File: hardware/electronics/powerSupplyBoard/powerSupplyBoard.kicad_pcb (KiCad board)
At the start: 4 copper layers, 100 x 50 mm, 119 parts, among them J1 USB_C_Receptacle_USB2.0, J10 1729018, J11 PREC002SAAN-RC, J3 615004143821, J4 PRPC009SBAN-M71RC, J5 Barrel_Jack_Switch, J6 S2B-PH-SM4-TB, J7 PREC002SAAN-RC, J8 PREC003SAAN-RC, J9 S3B-XH-SM4-TB, Q1 BUK961R6, Q2 CSD18532Q5B, Q3 CSD18532Q5B, Q4 BSS84, Q5 2N7002, Q6 2N7002, SW1 PTS647, SW2 SS-12D07, U1 STM32L052K6, U2 AP2112K-3.3, U3 SN65HVD230QDR, U4 BQ25798, U5 BQ76905, U6 BQ34Z100-R2, Y1 ECS-327ATQMV

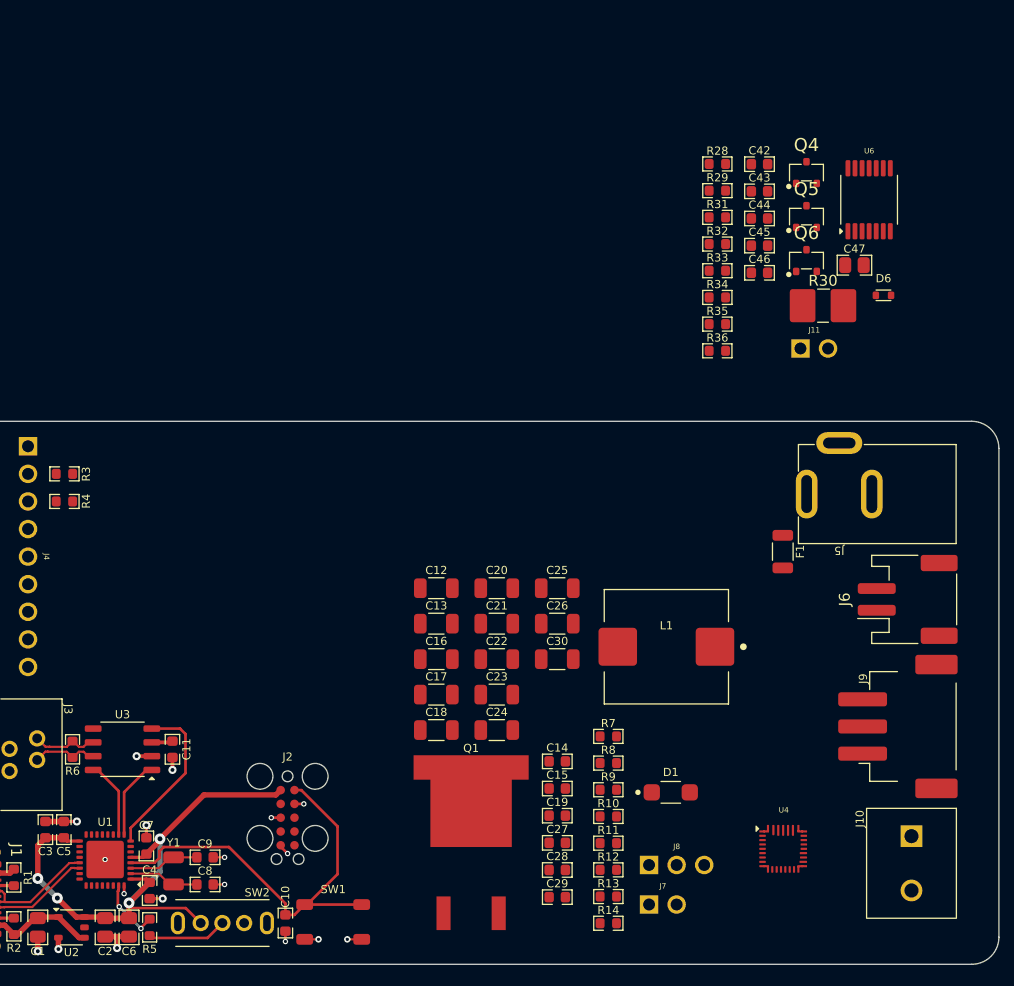
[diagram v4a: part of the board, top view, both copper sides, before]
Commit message: updated sch merger
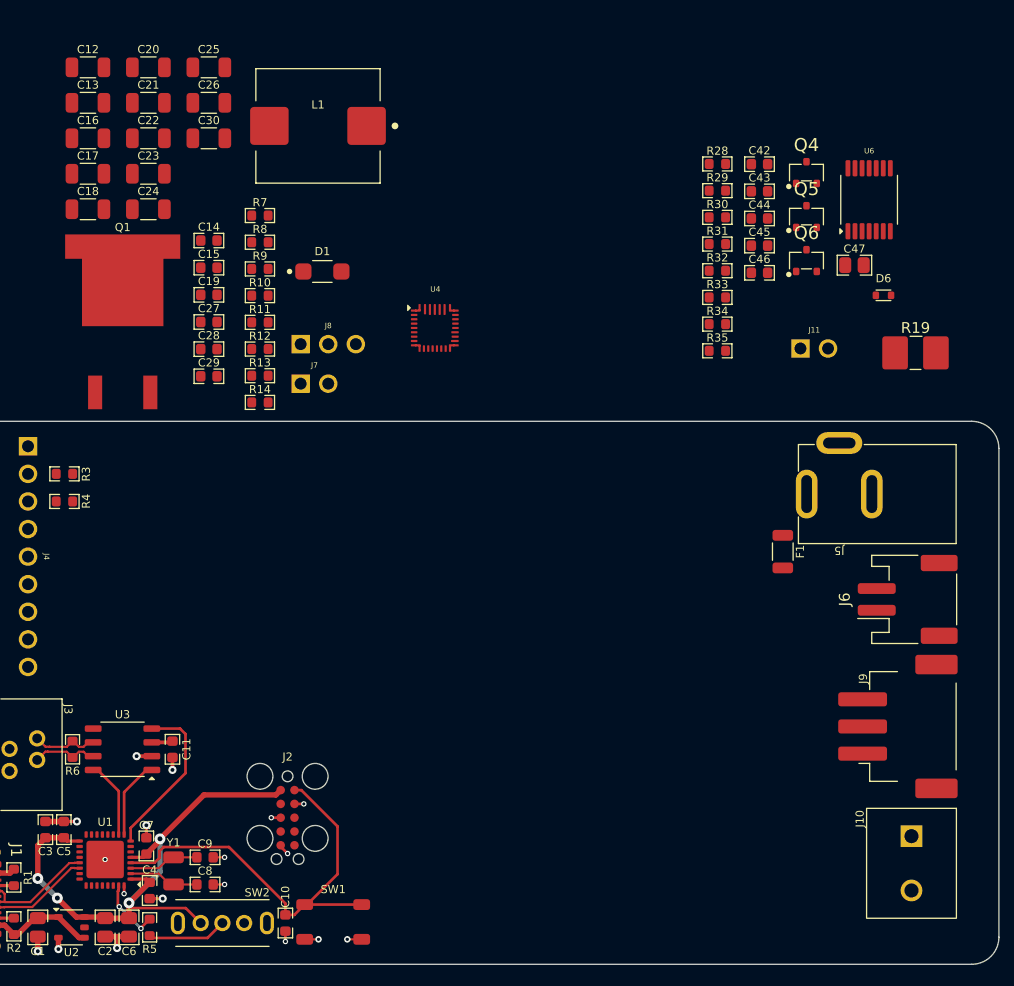
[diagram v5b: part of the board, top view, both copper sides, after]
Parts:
- removed the R30 at (168.8, 39.4)
- added R19: 30mR, DS-Resistors-SMD:WSLHP2010, F.Cu at (177.3, 43.7)
- moved C16 57.7 mm to (101.1, 23.9)
- moved C22 57.7 mm to (106.7, 23.9)
- moved C30 57.7 mm to (112.2, 23.9)
- moved J7 57.7 mm to (122.0, 46.5)
- moved Q1 57.7 mm to (104.3, 40.9)
- moved C13 57.7 mm to (101.1, 20.7)
- moved C14 57.7 mm to (112.3, 33.4)
- moved C15 57.7 mm to (112.3, 35.9)
- moved C18 57.7 mm to (101.1, 30.5)
- moved C19 57.7 mm to (112.3, 38.4)
- moved C21 57.7 mm to (106.7, 20.7)
- moved C24 57.7 mm to (106.7, 30.5)
- moved C26 57.7 mm to (112.2, 20.7)
- moved C27 57.7 mm to (112.3, 40.9)
- moved C28 57.7 mm to (112.3, 43.4)
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- renumbered R31 to R30, R32 to R31, R33 to R32, R34 to R33, R35 to R34, R36 to R35
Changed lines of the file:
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@@
 	(footprint "DS-Capacitors-SMD:MLCC1206"
 		(layer "F.Cu")
-		(at 133.198 75.166)
+		(at 101.118 27.206)
 		(descr "Capacitor, Chip; 3.20 mm L X 1.60 mm W X 0.88 mm H body")
 		(tags "1206; 3216")
@@
 	(footprint "DS-Capacitors-SMD:MLCC1206"
 		(layer "F.Cu")
-		(at 133.198 71.9)
+		(at 101.118 23.94)
 		(descr "Capacitor, Chip; 3.20 mm L X 1.60 mm W X 0.88 mm H body")
 		(tags "1206; 3216")
@@
 	(footprint "DS-Capacitors-SMD:MLCC0603"
 		(layer "F.Cu")
-		(at 144.335 88.815)
+		(at 112.255 40.855)
 		(descr "Capacitor, Chip; 1.60 mm L X 0.80 mm W X 0.88 mm H body")
 		(tags "0603; 1608")
@@
 	(footprint "DS-LED-SMD:LTST-1206"
 		(layer "F.Cu")
-		(at 154.785 84.165)
+		(at 122.705 36.205)
 		(descr "LED, Chip; 3.50 mm L X 2.20 mm W X 1.95 mm H body")
 		(property "Reference" "D1"
@@
 	(footprint "DS-Resistors-SMD:CRCW0603"
 		(layer "F.Cu")
-		(at 149.035 83.93)
+		(at 116.955 35.97)
 		(descr "Resistor, Chip; 1.60 mm L X 0.80 mm W X 0.55 mm H body")
 		(tags "0603; 1608")
@@
 	(footprint "DS-Resistors-SMD:CRCW0603"
 		(layer "F.Cu")
-		(at 149.035 86.388)
+		(at 116.955 38.428)
 		(descr "Resistor, Chip; 1.60 mm L X 0.80 mm W X 0.55 mm H body")
 		(tags "0603; 1608")
@@
 	(footprint "DS-Capacitors-SMD:MLCC1206"
 		(layer "F.Cu")
-		(at 138.764 75.166)
+		(at 106.684 27.206)
 		(descr "Capacitor, Chip; 3.20 mm L X 1.60 mm W X 0.88 mm H body")
 		(tags "1206; 3216")
@@
 	(footprint "DS-Resistors-SMD:WSLHP2010"
 		(layer "F.Cu")
-		(at 168.804 39.353)
+		(at 177.32 43.7)
 		(descr "Resistor, Chip; 5.08 mm L X 2.54 mm W X 0.889 mm H body")
-		(property "Reference" "R30"
+		(property "Reference" "R19"
 			(at 0 -2.3 0)
 			(layer "F.SilkS")
@@
 			)
 		)
-		(property "Value" "10mR"
+		(property "Value" "30mR"
 			(at 0 0 0)
 			(layer "User.1")
@@
 			)
 		)
-		(property "Description" "RES 0.01 OHM 1% 1W 2010"
+		(property "Description" "RES 0.03 OHM 1% 1W 2010"
 			(at 0 0 0)
 			(layer "F.Fab")
@@
 			)
 		)
-		(property "MPN" "WSL2010R0100FEA18"
+		(property "MPN" "WSL2010R0300FEA18"
 			(at 0 0 0)
 			(unlocked yes)
@@
 			)
 		)
-		(property "DKPN" "WSLF-.01CT-ND"
+		(property "DKPN" "WSLF-.03CT-ND"
 			(at 0 0 0)
 			(unlocked yes)
@@
 			)
 		)
-		(sheetname "Fuel Gauge")
-		(sheetfile "fuel_gauge.kicad_sch")
+		(sheetname "Battery Monitor")
+		(sheetfile "battery_monitor.kicad_sch")
 		(attr smd)
 		(fp_line
@@
 			(layers "F.Cu" "F.Paste" "F.Mask")
 			(roundrect_rratio 0.1059322034)
-			(net 23 "SENSE-")
+			(net 100 "SENSE+")
 			(pintype "passive")
 		)
@@
 			(layers "F.Cu" "F.Paste" "F.Mask")
 			(roundrect_rratio 0.1059322034)
-			(net 100 "SENSE+")
+			(net 23 "SENSE-")
 			(pintype "passive")
 		)
@@
 	(footprint "DS-Resistors-SMD:CRCW0603"
 		(layer "F.Cu")
-		(at 149.035 91.304)
+		(at 116.955 43.344)
 		(descr "Resistor, Chip; 1.60 mm L X 0.80 mm W X 0.55 mm H body")
 		(tags "0603; 1608")
@@
 		(descr "Resistor, Chip; 1.60 mm L X 0.80 mm W X 0.55 mm H body")
 		(tags "0603; 1608")
-		(property "Reference" "R36"
+		(property "Reference" "R35"
 			(at 0 -1.2 0)
 			(layer "F.SilkS")
@@
 	(footprint "DS-Capacitors-SMD:MLCC0603"
 		(layer "F.Cu")
-		(at 144.335 81.315)
+		(at 112.255 33.355)
 		(descr "Capacitor, Chip; 1.60 mm L X 0.80 mm W X 0.88 mm H body")
 		(tags "0603; 1608")
@@
 	(footprint "DS-Resistors-SMD:CRCW0603"
 		(layer "F.Cu")
-		(at 149.035 88.846)
+		(at 116.955 40.886)
 		(descr "Resistor, Chip; 1.60 mm L X 0.80 mm W X 0.55 mm H body")
 		(tags "0603; 1608")
@@
 	(footprint "DS-PMIC-SMD:RQM0029A"
 		(layer "F.Cu")
-		(at 165.135 89.365)
+		(at 133.055 41.405)
 		(property "Reference" "U4"
 			(at 0.05 -3.57 0)
@@
 	(footprint "DS-Capacitors-SMD:MLCC1206"
 		(layer "F.Cu")
-		(at 133.198 68.634)
+		(at 101.118 20.674)
 		(descr "Capacitor, Chip; 3.20 mm L X 1.60 mm W X 0.88 mm H body")
 		(tags "1206; 3216")
@@
 		(descr "Resistor, Chip; 1.60 mm L X 0.80 mm W X 0.55 mm H body")
 		(tags "0603; 1608")
-		(property "Reference" "R35"
+		(property "Reference" "R34"
 			(at 0 -1.2 0)
 			(layer "F.SilkS")
@@
 		(descr "Resistor, Chip; 1.60 mm L X 0.80 mm W X 0.55 mm H body")
 		(tags "0603; 1608")
-		(property "Reference" "R32"
+		(property "Reference" "R31"
 			(at 0 -1.2 0)
 			(layer "F.SilkS")
@@
 	(footprint "DS-Package-SO:SOT404"
 		(layer "F.Cu")
-		(at 136.4 88.9)
+		(at 104.32 40.94)
 		(property "Reference" "Q1"
 			(at 0 -8.8 0)
@@
 	(footprint "DS-Resistors-SMD:CRCW0603"
 		(layer "F.Cu")
-		(at 149.035 79.014)
+		(at 116.955 31.054)
 		(descr "Resistor, Chip; 1.60 mm L X 0.80 mm W X 0.55 mm H body")
 		(tags "0603; 1608")
@@
 	(footprint "DS-Capacitors-SMD:MLCC1206"
 		(layer "F.Cu")
-		(at 133.198 78.432)
+		(at 101.118 30.472)
 		(descr "Capacitor, Chip; 3.20 mm L X 1.60 mm W X 0.88 mm H body")
 		(tags "1206; 3216")
@@
 	(footprint "DS-Capacitors-SMD:MLCC1206"
 		(layer "F.Cu")
-		(at 133.198 65.368)
+		(at 101.118 17.408)
 		(descr "Capacitor, Chip; 3.20 mm L X 1.60 mm W X 0.88 mm H body")
 		(tags "1206; 3216")
@@
 	(footprint "DS-Capacitors-SMD:MLCC1206"
 		(layer "F.Cu")
-		(at 144.33 71.9)
+		(at 112.25 23.94)
 		(descr "Capacitor, Chip; 3.20 mm L X 1.60 mm W X 0.88 mm H body")
 		(tags "1206; 3216")
@@
 	(footprint "DS-Capacitors-SMD:MLCC1206"
 		(layer "F.Cu")
-		(at 138.764 65.368)
+		(at 106.684 17.408)
 		(descr "Capacitor, Chip; 3.20 mm L X 1.60 mm W X 0.88 mm H body")
 		(tags "1206; 3216")
@@
 	(footprint "DS-Capacitors-SMD:MLCC1206"
 		(layer "F.Cu")
-		(at 138.764 68.634)
+		(at 106.684 20.674)
 		(descr "Capacitor, Chip; 3.20 mm L X 1.60 mm W X 0.88 mm H body")
 		(tags "1206; 3216")
@@
 	(footprint "DS-Capacitors-SMD:MLCC0603"
 		(layer "F.Cu")
-		(at 144.335 86.315)
+		(at 112.255 38.355)
 		(descr "Capacitor, Chip; 1.60 mm L X 0.80 mm W X 0.88 mm H body")
 		(tags "0603; 1608")
@@
 		(descr "Resistor, Chip; 1.60 mm L X 0.80 mm W X 0.55 mm H body")
 		(tags "0603; 1608")
-		(property "Reference" "R34"
+		(property "Reference" "R33"
 			(at 0 -1.2 0)
 			(layer "F.SilkS")
@@
 	(footprint "DS-Capacitors-SMD:MLCC0603"
 		(layer "F.Cu")
-		(at 144.335 93.815)
+		(at 112.255 45.855)
 		(descr "Capacitor, Chip; 1.60 mm L X 0.80 mm W X 0.88 mm H body")
 		(tags "0603; 1608")
@@
 	(footprint "DS-Capacitors-SMD:MLCC1206"
 		(layer "F.Cu")
-		(at 138.764 71.9)
+		(at 106.684 23.94)
 		(descr "Capacitor, Chip; 3.20 mm L X 1.60 mm W X 0.88 mm H body")
 		(tags "1206; 3216")
@@
 	(footprint "DS-Capacitors-SMD:MLCC1206"
 		(layer "F.Cu")
-		(at 138.764 78.432)
+		(at 106.684 30.472)
 		(descr "Capacitor, Chip; 3.20 mm L X 1.60 mm W X 0.88 mm H body")
 		(tags "1206; 3216")
@@
 	(footprint "DS-Resistors-SMD:CRCW0603"
 		(layer "F.Cu")
-		(at 149.035 81.472)
+		(at 116.955 33.512)
 		(descr "Resistor, Chip; 1.60 mm L X 0.80 mm W X 0.55 mm H body")
 		(tags "0603; 1608")
@@
 	(footprint "DS-Rectangular-Connectors:conn_01x03_254"
 		(layer "F.Cu")
-		(at 155.325 90.855)
+		(at 123.245 42.895)
 		(property "Reference" "J8"
 			(at 0 -1.7 0)
@@
 	(footprint "DS-Capacitors-SMD:MLCC1206"
 		(layer "F.Cu")
-		(at 144.33 68.634)
+		(at 112.25 20.674)
 		(descr "Capacitor, Chip; 3.20 mm L X 1.60 mm W X 0.88 mm H body")
 		(tags "1206; 3216")
@@
 	(footprint "DS-Resistors-SMD:CRCW0603"
 		(layer "F.Cu")
-		(at 149.035 93.762)
+		(at 116.955 45.802)
 		(descr "Resistor, Chip; 1.60 mm L X 0.80 mm W X 0.55 mm H body")
 		(tags "0603; 1608")
@@
 	(footprint "DS-Capacitors-SMD:MLCC0603"
 		(layer "F.Cu")
-		(at 144.335 91.315)
+		(at 112.255 43.355)
 		(descr "Capacitor, Chip; 1.60 mm L X 0.80 mm W X 0.88 mm H body")
 		(tags "0603; 1608")
@@
 	(footprint "DS-Rectangular-Connectors:conn_01x02_254"
 		(layer "F.Cu")
-		(at 154.055 94.495)
+		(at 121.975 46.535)
 		(property "Reference" "J7"
 			(at 0 -1.7 0)
@@
 	(footprint "DS-Capacitors-SMD:MLCC0603"
 		(layer "F.Cu")
-		(at 144.335 83.815)
+		(at 112.255 35.855)
 		(descr "Capacitor, Chip; 1.60 mm L X 0.80 mm W X 0.88 mm H body")
 		(tags "0603; 1608")
@@
 	(footprint "DS-Resistors-SMD:CRCW0603"
 		(layer "F.Cu")
-		(at 149.035 96.22)
+		(at 116.955 48.26)
 		(descr "Resistor, Chip; 1.60 mm L X 0.80 mm W X 0.55 mm H body")
 		(tags "0603; 1608")
@@
 	(footprint "DS-Capacitors-SMD:MLCC1206"
 		(layer "F.Cu")
-		(at 144.33 65.368)
+		(at 112.25 17.408)
 		(descr "Capacitor, Chip; 3.20 mm L X 1.60 mm W X 0.88 mm H body")
 		(tags "1206; 3216")
@@
 	(footprint "DS-Inductors-SMD:HCM1A1105V2"
 		(layer "F.Cu")
-		(at 154.38 70.76)
+		(at 122.3 22.8)
 		(descr "Inductor, Chip; 2.50 mm L X 2.00 mm W X 1.20 mm H body")
 		(property "Reference" "L1"
@@
 		(descr "Resistor, Chip; 1.60 mm L X 0.80 mm W X 0.55 mm H body")
 		(tags "0603; 1608")
-		(property "Reference" "R33"
+		(property "Reference" "R32"
 			(at 0 -1.2 0)
 			(layer "F.SilkS")
@@
 		(descr "Resistor, Chip; 1.60 mm L X 0.80 mm W X 0.55 mm H body")
 		(tags "0603; 1608")
-		(property "Reference" "R31"
+		(property "Reference" "R30"
 			(at 0 -1.2 0)
 			(layer "F.SilkS")

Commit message: fixed GPIO header power net
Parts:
- R32: value 165K -> 14K
- R33: value 133K -> 100K
- R34: value 16K5 -> 14K
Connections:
- J4 pad 1: /VUSB -> +3V3
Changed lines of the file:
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@@
 			(layers "*.Cu" "*.Mask")
 			(remove_unused_layers no)
-			(net 88 "/VUSB")
+			(net 3 "+3V3")
 			(pintype "passive")
 		)
@@
 			)
 		)
-		(property "Value" "16K5"
+		(property "Value" "14K"
 			(at 0 0 0)
 			(layer "User.1")
@@
 			)
 		)
-		(property "Description" "RES 16.5K OHM 0.1% 0.21W 0603"
+		(property "Description" "RES 14K OHM 0.1% 0.21W 0603"
 			(at 0 0 0)
 			(layer "F.Fab")
@@
 			)
 		)
-		(property "MPN" "TNPW060316K5BEEA"
+		(property "MPN" "TNPW060314K0BEEA"
 			(at 0 0 0)
 			(unlocked yes)
@@
 			)
 		)
-		(property "DKPN" "541-3172-1-ND"
+		(property "DKPN" "TNP14.0KAACT-ND"
 			(at 0 0 0)
 			(unlocked yes)
@@
 			)
 		)
-		(property "Value" "133K"
+		(property "Value" "100K"
 			(at 0 0 0)
 			(layer "User.1")
@@
 			)
 		)
-		(property "Description" "RES 133K OHM 0.1% 0.21W 0603"
+		(property "Description" "RES 100K OHM 0.1% 0.21W 0603"
 			(at 0 0 0)
 			(layer "F.Fab")
@@
 			)
 		)
-		(property "MPN" "TNPW0603133KBEEA"
+		(property "MPN" "TNPW0603100KBEEA"
 			(at 0 0 0)
 			(unlocked yes)
@@
 			)
 		)
-		(property "DKPN" "541-TNPW0603133KBEEACT-ND"
+		(property "DKPN" "TNP100KAACT-ND"
 			(at 0 0 0)
 			(unlocked yes)
@@
 			)
 		)
-		(property "Datasheet" "datasheets/Texas-Instruments-BQ34Z100-R2"
+		(property "Datasheet" "datasheets/Texas-Instruments-BQ34Z100-R2.pdf"
 			(at 0 0 0)
 			(layer "F.Fab")
@@
 			)
 		)
-		(property "Value" "165K"
+		(property "Value" "14K"
 			(at 0 0 0)
 			(layer "User.1")
@@
 			)
 		)
-		(property "Description" "RES SMD 165K OHM 1% 1/10W 0603"
+		(property "Description" "RES SMD 14K OHM 1% 1/10W 0603"
 			(at 0 0 0)
 			(layer "F.Fab")
@@
 			)
 		)
-		(property "MPN" "CRCW0603165KFKEA"
+		(property "MPN" "CRCW060314K0FKEA"
 			(at 0 0 0)
 			(unlocked yes)
@@
 			)
 		)
-		(property "DKPN" "541-165KHCT-ND"
+		(property "DKPN" "541-14.0KHCT-ND"
 			(at 0 0 0)
 			(unlocked yes)
